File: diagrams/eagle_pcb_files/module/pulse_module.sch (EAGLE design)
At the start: 4 parts

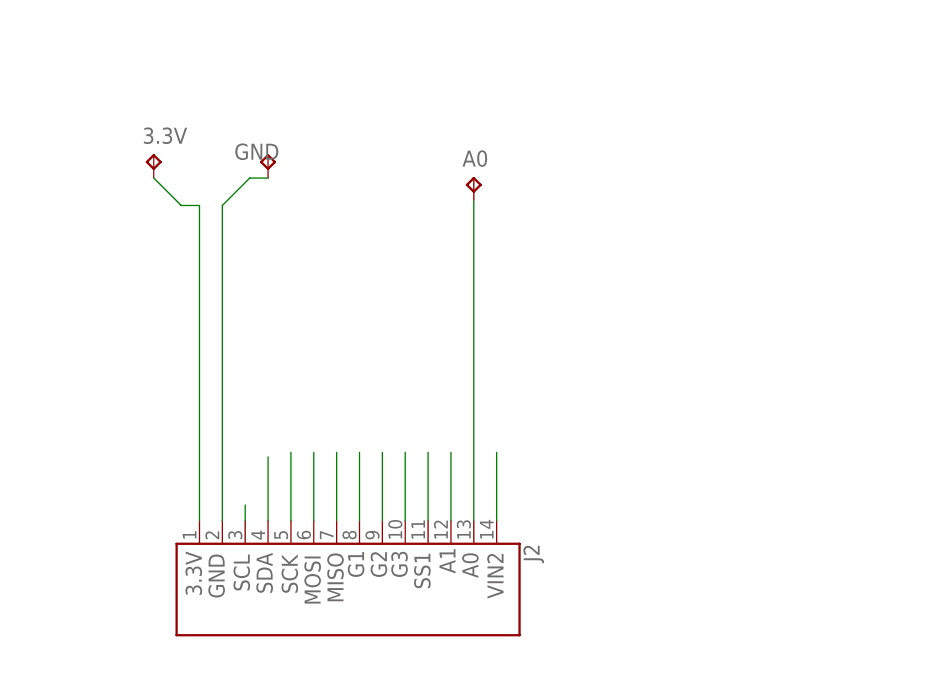
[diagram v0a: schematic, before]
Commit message: GND plane, add 100nF cap
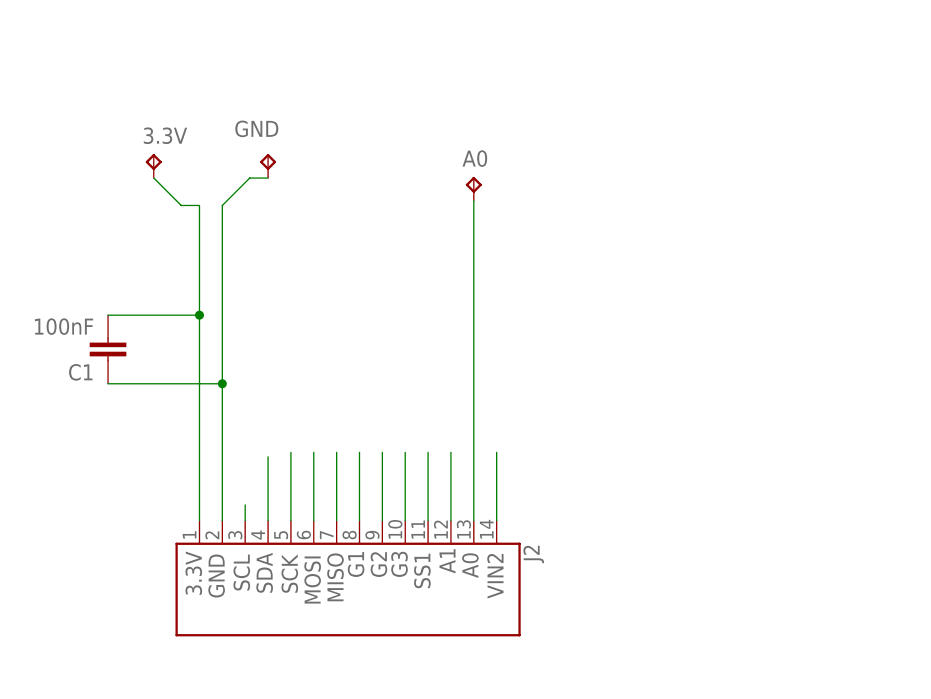
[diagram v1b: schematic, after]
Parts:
- added C1: 100nF, rcl:C-EUC1206
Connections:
- net 3.3V: now also C1.2
- net GND: now also C1.1
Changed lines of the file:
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@@
 <part name="GND" library="testpad" library_urn="urn:adsk.eagle:library:385" deviceset="TP" device="TP20R" package3d_urn="urn:adsk.eagle:package:27973/1"/>
 <part name="A0" library="testpad" library_urn="urn:adsk.eagle:library:385" deviceset="TP" device="TP20R" package3d_urn="urn:adsk.eagle:package:27973/1"/>
+<part name="C1" library="rcl" library_urn="urn:adsk.eagle:library:334" deviceset="C-EU" device="C1206" package3d_urn="urn:adsk.eagle:package:23618/2" value="100nF"/>
 </parts>
 <sheets>
@@
 </instance>
 <instance part="GND" gate="G$1" x="73.66" y="78.74" smashed="yes">
-<attribute name="NAME" x="74.93" y="80.01" size="1.778" layer="95" rot="R180"/>
+<attribute name="NAME" x="74.93" y="82.55" size="1.778" layer="95" rot="R180"/>
 <attribute name="TP_SIGNAL_NAME" x="74.93" y="77.47" size="1.778" layer="97"/>
 </instance>
@@
 <attribute name="NAME" x="95.25" y="77.47" size="1.778" layer="95"/>
 <attribute name="TP_SIGNAL_NAME" x="97.79" y="74.93" size="1.778" layer="97"/>
+</instance>
+<instance part="C1" gate="G$1" x="55.88" y="55.88" smashed="yes" rot="R180">
+<attribute name="NAME" x="54.356" y="55.499" size="1.778" layer="95" rot="R180"/>
+<attribute name="VALUE" x="54.356" y="60.579" size="1.778" layer="96" rot="R180"/>
 </instance>
 </instances>
@@
 <label x="68.834" y="29.464" size="1.778" layer="95" rot="R90"/>
 <pinref part="J2" gate="G$1" pin="13"/>
-<wire x1="68.58" y1="73.152" x2="68.58" y2="38.1" width="0.1524" layer="91"/>
+<wire x1="68.58" y1="73.152" x2="68.58" y2="53.34" width="0.1524" layer="91"/>
 <pinref part="GND" gate="G$1" pin="TP"/>
+<wire x1="68.58" y1="53.34" x2="68.58" y2="38.1" width="0.1524" layer="91"/>
 <wire x1="68.58" y1="73.152" x2="71.628" y2="76.2" width="0.1524" layer="91"/>
 <wire x1="71.628" y1="76.2" x2="73.66" y2="76.2" width="0.1524" layer="91"/>
+<pinref part="C1" gate="G$1" pin="1"/>
+<wire x1="55.88" y1="53.34" x2="68.58" y2="53.34" width="0.1524" layer="91"/>
+<junction x="68.58" y="53.34"/>
 </segment>
 </net>
@@
 <pinref part="J2" gate="G$1" pin="14"/>
 <label x="66.294" y="29.718" size="1.778" layer="95" rot="R90"/>
-<wire x1="66.04" y1="38.1" x2="66.04" y2="73.152" width="0.1524" layer="91"/>
+<wire x1="66.04" y1="38.1" x2="66.04" y2="60.96" width="0.1524" layer="91"/>
 <pinref part="3.3V" gate="G$1" pin="TP"/>
+<wire x1="66.04" y1="60.96" x2="66.04" y2="73.152" width="0.1524" layer="91"/>
 <wire x1="60.96" y1="76.2" x2="64.008" y2="73.152" width="0.1524" layer="91"/>
 <wire x1="64.008" y1="73.152" x2="66.04" y2="73.152" width="0.1524" layer="91"/>
+<pinref part="C1" gate="G$1" pin="2"/>
+<wire x1="55.88" y1="60.96" x2="66.04" y2="60.96" width="0.1524" layer="91"/>
+<junction x="66.04" y="60.96"/>
 </segment>
 </net>
@@
 packages will not be understood (or retained) with this version.
 </note>
+<note version="8.4" severity="warning">
+Since Version 8.4, EAGLE supports properties for SPICE simulation.
+Probes in schematics and SPICE mapping objects found in parts and library devices
+will not be understood with this version. Update EAGLE to the latest version
+for full support of SPICE simulation.
+</note>
 </compatibility>

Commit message: pulse module board with adc
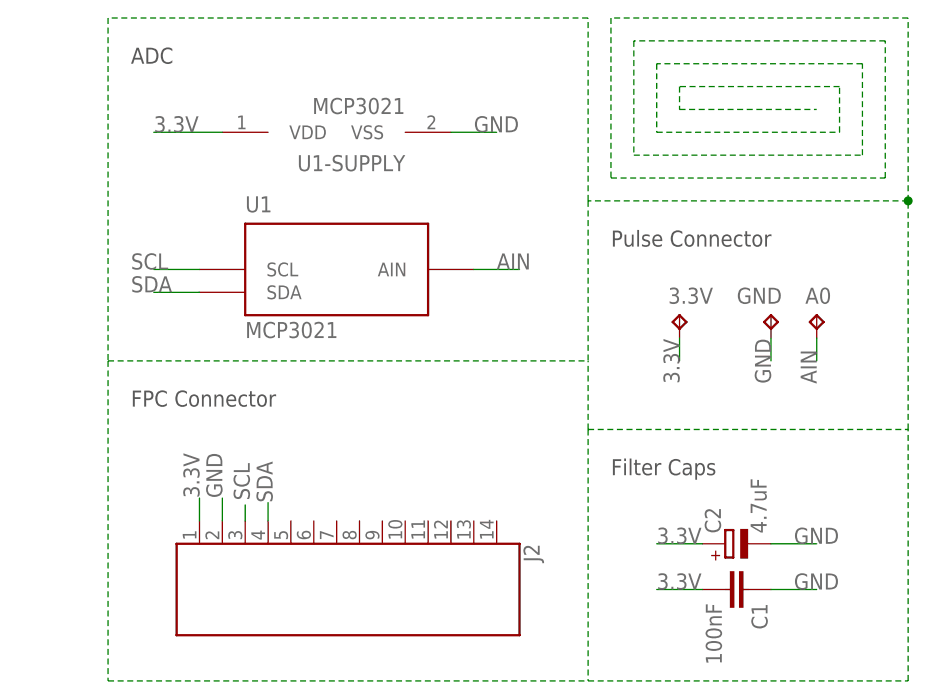
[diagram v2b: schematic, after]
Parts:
- added C2: 4.7uF, rcl:CPOL-EUSMCA
- added U1: MCP3021, Volks73-MicrochipTechnology:MCP3021
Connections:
- removed net A0: A0.TP, J2.2
- removed net A1: J2.3
- removed net G1: J2.7
- removed net G2: J2.6
- removed net G3: J2.5
- removed net MISO: J2.8
- removed net MOSI: J2.9
- removed net SCK: J2.10
- removed net SS1: J2.4
- removed net VIN2: J2.1
- new net AIN: A0.TP, U1U$1.AIN
- net 3.3V: now also C2.+, U1-SUPPLY.VDD
- net GND: now also C2.-, U1-SUPPLY.VSS
- net SCL: now also U1U$1.SCL
- net SDA: now also U1U$1.SDA
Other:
- note added: "ADC"
- note added: "FPC Connector"
- note added: "Filter Caps"
- note added: "Pulse Connector"
- moved on the sheet: 3.3V, A0, C1, GND
